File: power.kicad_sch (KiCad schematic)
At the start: 33 parts, among them Q6 PNP

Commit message: updated pcb
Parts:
- J?: footprint AMASS_XT30PW-M -> Connector_AMASS:AMASS_XT30PW-M_1x02_P2.50mm_Horizontal
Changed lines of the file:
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@@
       (effects (font (size 1.27 1.27)))
     )
-    (property "Footprint" "AMASS_XT30PW-M" (at 190.5 73.66 0)
+    (property "Footprint" "Connector_AMASS:AMASS_XT30PW-M_1x02_P2.50mm_Horizontal" (at 190.5 73.66 0)
       (effects (font (size 1.27 1.27)) (justify bottom) hide)
     )

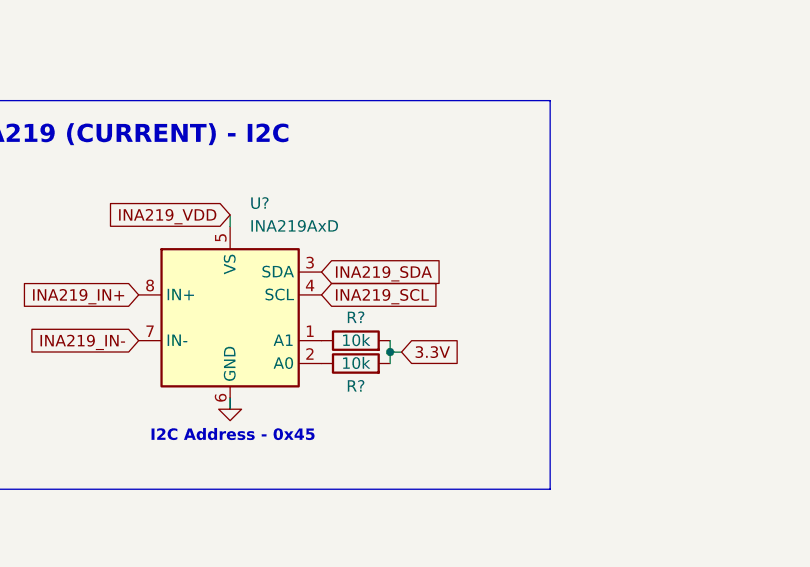
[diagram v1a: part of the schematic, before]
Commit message: grouped components
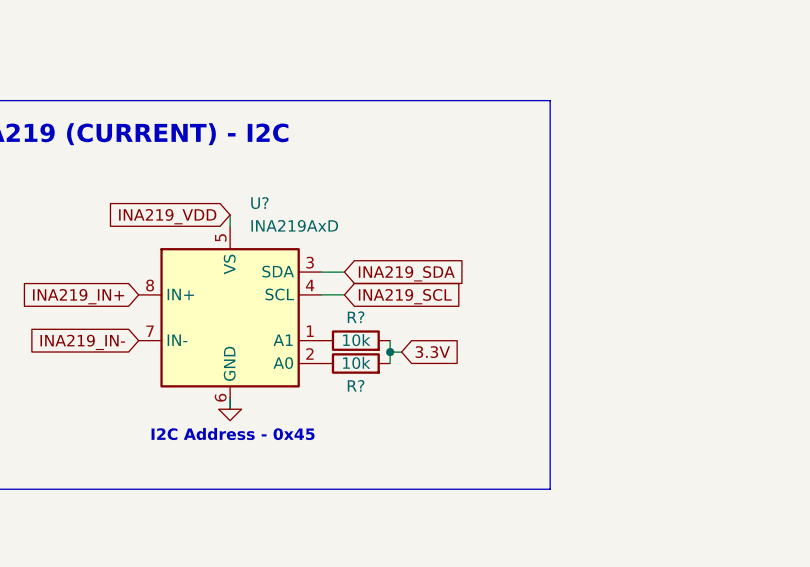
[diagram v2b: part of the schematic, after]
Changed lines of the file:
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@@
+    (stroke (width 0) (type default))
+  )
+  (wire (pts (xy 191.77 124.46) (xy 194.31 124.46))
     (stroke (width 0) (type default))
   )
@@
   )
   (wire (pts (xy 95.25 76.2) (xy 95.25 80.01))
+    (stroke (width 0) (type default))
+  )
+  (wire (pts (xy 191.77 121.92) (xy 194.31 121.92))
     (stroke (width 0) (type default))
   )
@@
     )
   )
+  (global_label "INA219_SCL" (shape input) (at 194.31 124.46 0) (fields_autoplaced)
+    (effects (font (size 1.27 1.27)) (justify left))
+    (property "Intersheetrefs" "${INTERSHEET_REFS}" (at 208.4228 124.46 0)
+      (effects (font (size 1.27 1.27)) (justify left) hide)
+    )
+  )
   (global_label "INA219_IN+" (shape input) (at 196.85 73.66 90) (fields_autoplaced)
     (effects (font (size 1.27 1.27)) (justify left))
@@
     )
   )
-  (global_label "INA219_SDA" (shape input) (at 191.77 121.92 0) (fields_autoplaced)
-    (effects (font (size 1.27 1.27)) (justify left))
-    (property "Intersheetrefs" "${INTERSHEET_REFS}" (at 205.9433 121.92 0)
-      (effects (font (size 1.27 1.27)) (justify left) hide)
-    )
-  )
   (global_label "INA219_IN-" (shape input) (at 171.45 129.54 180) (fields_autoplaced)
     (effects (font (size 1.27 1.27)) (justify right))
@@
     )
   )
-  (global_label "INA219_SCL" (shape input) (at 191.77 124.46 0) (fields_autoplaced)
-    (effects (font (size 1.27 1.27)) (justify left))
-    (property "Intersheetrefs" "${INTERSHEET_REFS}" (at 205.8828 124.46 0)
-      (effects (font (size 1.27 1.27)) (justify left) hide)
-    )
-  )
   (global_label "VIN" (shape input) (at 44.45 127 180) (fields_autoplaced)
     (effects (font (size 1.27 1.27)) (justify right))
@@
     )
   )
+  (global_label "INA219_SDA" (shape input) (at 194.31 121.92 0) (fields_autoplaced)
+    (effects (font (size 1.27 1.27)) (justify left))
+    (property "Intersheetrefs" "${INTERSHEET_REFS}" (at 208.4833 121.92 0)
+      (effects (font (size 1.27 1.27)) (justify left) hide)
+    )
+  )

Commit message: started routing
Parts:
- R? (x2): footprint Resistor_SMD:R_0603_1608Metric -> Resistor_SMD:R_0402_1005Metric
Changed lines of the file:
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@@
       (effects (font (size 1.27 1.27)))
     )
-    (property "Footprint" "Resistor_SMD:R_0603_1608Metric" (at 195.58 131.318 90)
+    (property "Footprint" "Resistor_SMD:R_0402_1005Metric" (at 195.58 131.318 90)
       (effects (font (size 1.27 1.27)) hide)
     )
@@
       (effects (font (size 1.27 1.27)))
     )
-    (property "Footprint" "Resistor_SMD:R_0603_1608Metric" (at 195.58 133.858 90)
-      (effects (font (size 1.27 1.27)) hide)
-    )
+    (property "Footprint" "Resistor_SMD:R_0402_1005Metric" (at 195.58 133.858 90)
+      (effects (font (size 1.27 1.27)) hide)
+    )

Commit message: updated schematic
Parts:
- removed Q6: PNP, Package_TO_SOT_SMD:SOT-23, symbol Simulation_SPICE:PNP
- added Q6: Q_PMOS_GDS, Package_TO_SOT_SMD:SOT-23, symbol Device:Q_PMOS_GDS
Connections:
- net INA219_IN-: now also Q6.2 (D)
- net VBUS: now also Q6.1 (G)
- net VIN: now also Q6.3 (S)
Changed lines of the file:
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@@
-    )
-  )
-  (symbol (lib_id "Simulation_SPICE:PNP") (at 144.78 66.04 0) (unit 1)
-    (in_bom yes) (on_board yes) (dnp no) (fields_autoplaced)
-    (property "Reference" "Q6" (at 149.86 64.77 0)
-      (effects (font (size 1.27 1.27)) (justify left))
-    )
-    (property "Value" "PNP" (at 149.86 67.31 0)
-      (effects (font (size 1.27 1.27)) (justify left))
-    )
-    (property "Footprint" "Package_TO_SOT_SMD:SOT-23" (at 180.34 66.04 0)
-      (effects (font (size 1.27 1.27)) hide)
-    )
-    (property "Datasheet" "~" (at 180.34 66.04 0)
-      (effects (font (size 1.27 1.27)) hide)
-    )
-    (property "Sim.Device" "PNP" (at 144.78 66.04 0)
-      (effects (font (size 1.27 1.27)) hide)
-    )
-    (property "Sim.Type" "GUMMELPOON" (at 144.78 66.04 0)
-      (effects (font (size 1.27 1.27)) hide)
-    )
-    (property "Sim.Pins" "1=C 2=B 3=E" (at 144.78 66.04 0)
-      (effects (font (size 1.27 1.27)) hide)
-    )
-    (pin "1")
-    (pin "2")
-    (pin "3")
-    (instances
-      (project "aether"
-        (path "/e12346fa-509d-4de9-8ab1-dced307292db/c23bfb85-0f05-40d7-b8da-b36b200d10d9"
-          (reference "Q6") (unit 1)
-        )
-      )
     )
   )
@@
   )
   (symbol (lib_id "Device:R") (at 135.89 81.28 0) (unit 1)
-    (in_bom yes) (on_board yes) (dnp no) (fields_autoplaced)
-    (property "Reference" "R?" (at 138.43 80.01 0)
-      (effects (font (size 1.27 1.27)) (justify left))
-    )
-    (property "Value" "100k" (at 138.43 82.55 0)
+    (in_bom yes) (on_board yes) (dnp no)
+    (property "Reference" "R?" (at 127 80.01 0)
+      (effects (font (size 1.27 1.27)) (justify left))
+    )
+    (property "Value" "100k" (at 127 82.55 0)
       (effects (font (size 1.27 1.27)) (justify left))
     )
@@
         )
       )
+    )
+  )
+  (symbol (lib_id "Device:Q_PMOS_GDS") (at 144.78 66.04 0) (unit 1)
+    (in_bom yes) (on_board yes) (dnp no) (fields_autoplaced)
+    (property "Reference" "Q6" (at 151.13 64.77 0)
+      (effects (font (size 1.27 1.27)) (justify left))
+    )
+    (property "Value" "Q_PMOS_GDS" (at 151.13 67.31 0)
+      (effects (font (size 1.27 1.27)) (justify left))
+    )
+    (property "Footprint" "Package_TO_SOT_SMD:SOT-23" (at 149.86 63.5 0)
+      (effects (font (size 1.27 1.27)) hide)
+    )
+    (property "Datasheet" "~" (at 144.78 66.04 0)
+      (effects (font (size 1.27 1.27)) hide)
+    )
+    (pin "1")
+    (pin "2")
+    (pin "3")
+    (instances
+      (project "aether"
+        (path "/e12346fa-509d-4de9-8ab1-dced307292db/c23bfb85-0f05-40d7-b8da-b36b200d10d9"
+          (reference "Q6") (unit 1)
+        )
+      )
